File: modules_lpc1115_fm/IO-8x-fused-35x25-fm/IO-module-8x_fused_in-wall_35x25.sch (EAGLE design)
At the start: 83 parts, among them IC1 LPC1115, IC2 ATAES132A-SHEQ-T, Q2 ASFL, U1 EEPROM, X3 MICROMATCH-10

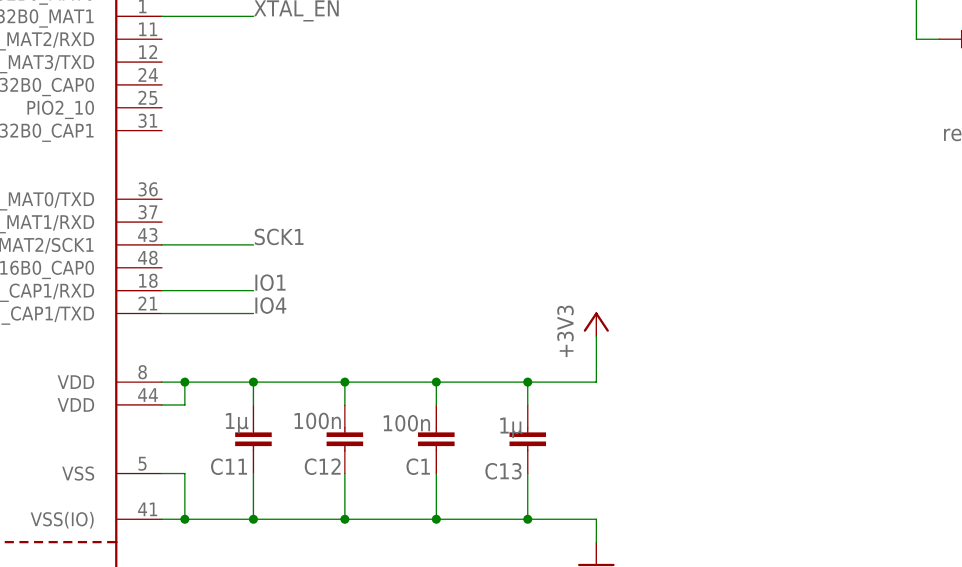
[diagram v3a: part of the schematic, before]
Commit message: [IOmodule8xUP] added debug RXD / TXD / GND solder pads
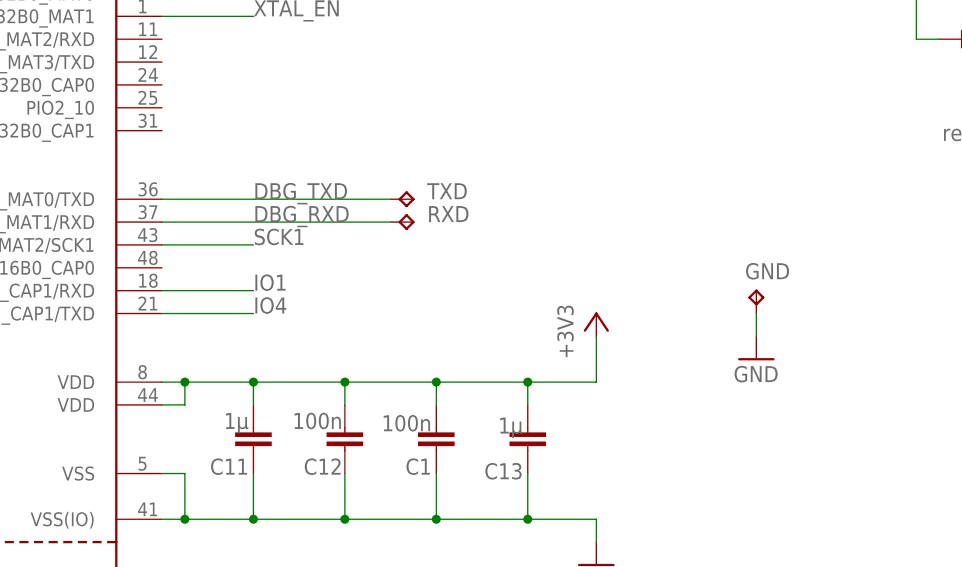
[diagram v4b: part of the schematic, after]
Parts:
- added GND: TPTP11SQ, testpad:TPTP11SQ
- added RXD: TPTP12R, testpad:TPTP12R
- added TXD: TPTP12SQ, testpad:TPTP12SQ
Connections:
- new net DBG_RXD: IC1.PIO3_1/DSR/CT16B0_MAT1/RXD, RXD.TP
- new net DBG_TXD: IC1.PIO3_0/DTR/CT16B0_MAT0/TXD, TXD.TP
- net GND: now also GND.TP
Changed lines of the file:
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@@
 <?xml version="1.0" encoding="utf-8"?>
 <!DOCTYPE eagle SYSTEM "eagle.dtd">
-<eagle version="9.6.1">
+<eagle version="9.6.2">
 <drawing>
 <settings>
@@
 <part name="P+12" library="supply1" deviceset="+3V3" device=""/>
 <part name="GND5" library="supply1" deviceset="GND" device=""/>
+<part name="TXD" library="testpad" library_urn="urn:adsk.eagle:library:385" deviceset="TP" device="TP12SQ" package3d_urn="urn:adsk.eagle:package:27964/1" value="TPTP12SQ"/>
+<part name="RXD" library="testpad" library_urn="urn:adsk.eagle:library:385" deviceset="TP" device="TP12R" package3d_urn="urn:adsk.eagle:package:27963/1" value="TPTP12R"/>
+<part name="GND" library="testpad" library_urn="urn:adsk.eagle:library:385" deviceset="TP" device="TP11SQ" package3d_urn="urn:adsk.eagle:package:27965/1" value="TPTP11SQ"/>
+<part name="GND7" library="supply1" deviceset="GND" device=""/>
 </parts>
 <sheets>
@@
 <instance part="GND5" gate="1" x="609.6" y="38.1" smashed="yes">
 <attribute name="VALUE" x="607.06" y="35.56" size="1.778" layer="96"/>
+</instance>
+<instance part="TXD" gate="G$1" x="434.34" y="137.16" smashed="yes" rot="R270">
+<attribute name="NAME" x="435.864" y="137.16" size="1.778" layer="95"/>
+<attribute name="TP_SIGNAL_NAME" x="433.07" y="135.89" size="1.778" layer="97" rot="R270"/>
+</instance>
+<instance part="RXD" gate="G$1" x="434.34" y="134.62" smashed="yes" rot="R270">
+<attribute name="NAME" x="435.864" y="134.62" size="1.778" layer="95"/>
+<attribute name="TP_SIGNAL_NAME" x="433.07" y="133.35" size="1.778" layer="97" rot="R270"/>
+</instance>
+<instance part="GND" gate="G$1" x="472.44" y="127" smashed="yes">
+<attribute name="NAME" x="471.17" y="128.27" size="1.778" layer="95"/>
+<attribute name="TP_SIGNAL_NAME" x="473.71" y="125.73" size="1.778" layer="97"/>
+</instance>
+<instance part="GND7" gate="1" x="472.44" y="119.38" smashed="yes">
+<attribute name="VALUE" x="469.9" y="116.84" size="1.778" layer="96"/>
 </instance>
 </instances>
@@
 <wire x1="523.24" y1="132.08" x2="523.24" y2="127" width="0.1524" layer="91"/>
 </segment>
+<segment>
+<pinref part="GND" gate="G$1" pin="TP"/>
+<pinref part="GND7" gate="1" pin="GND"/>
+<wire x1="472.44" y1="124.46" x2="472.44" y2="121.92" width="0.1524" layer="91"/>
+</segment>
 </net>
 <net name="EIB_OUT" class="0">
@@
 </segment>
 </net>
+<net name="DBG_TXD" class="0">
+<segment>
+<pinref part="IC1" gate="G$1" pin="PIO3_0/DTR/CT16B0_MAT0/TXD"/>
+<label x="416.56" y="137.16" size="1.778" layer="95"/>
+<wire x1="406.4" y1="137.16" x2="431.8" y2="137.16" width="0.1524" layer="91"/>
+<pinref part="TXD" gate="G$1" pin="TP"/>
+</segment>
+</net>
+<net name="DBG_RXD" class="0">
+<segment>
+<pinref part="IC1" gate="G$1" pin="PIO3_1/DSR/CT16B0_MAT1/RXD"/>
+<label x="416.56" y="134.62" size="1.778" layer="95"/>
+<wire x1="406.4" y1="134.62" x2="431.8" y2="134.62" width="0.1524" layer="91"/>
+<pinref part="RXD" gate="G$1" pin="TP"/>
+</segment>
+</net>

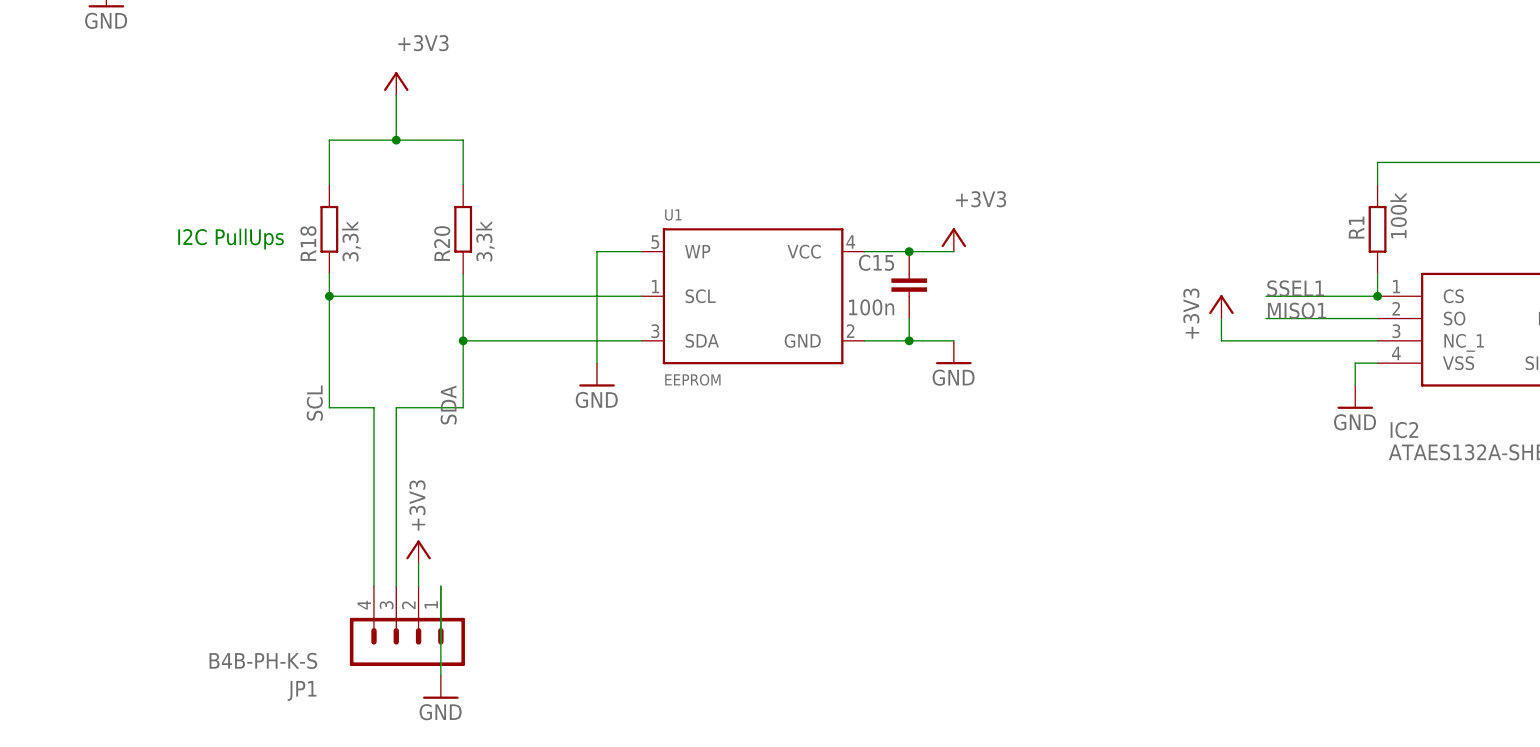
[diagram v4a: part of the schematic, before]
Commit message: [IOmodule8xUP] added missing blocking capacitor to IC2
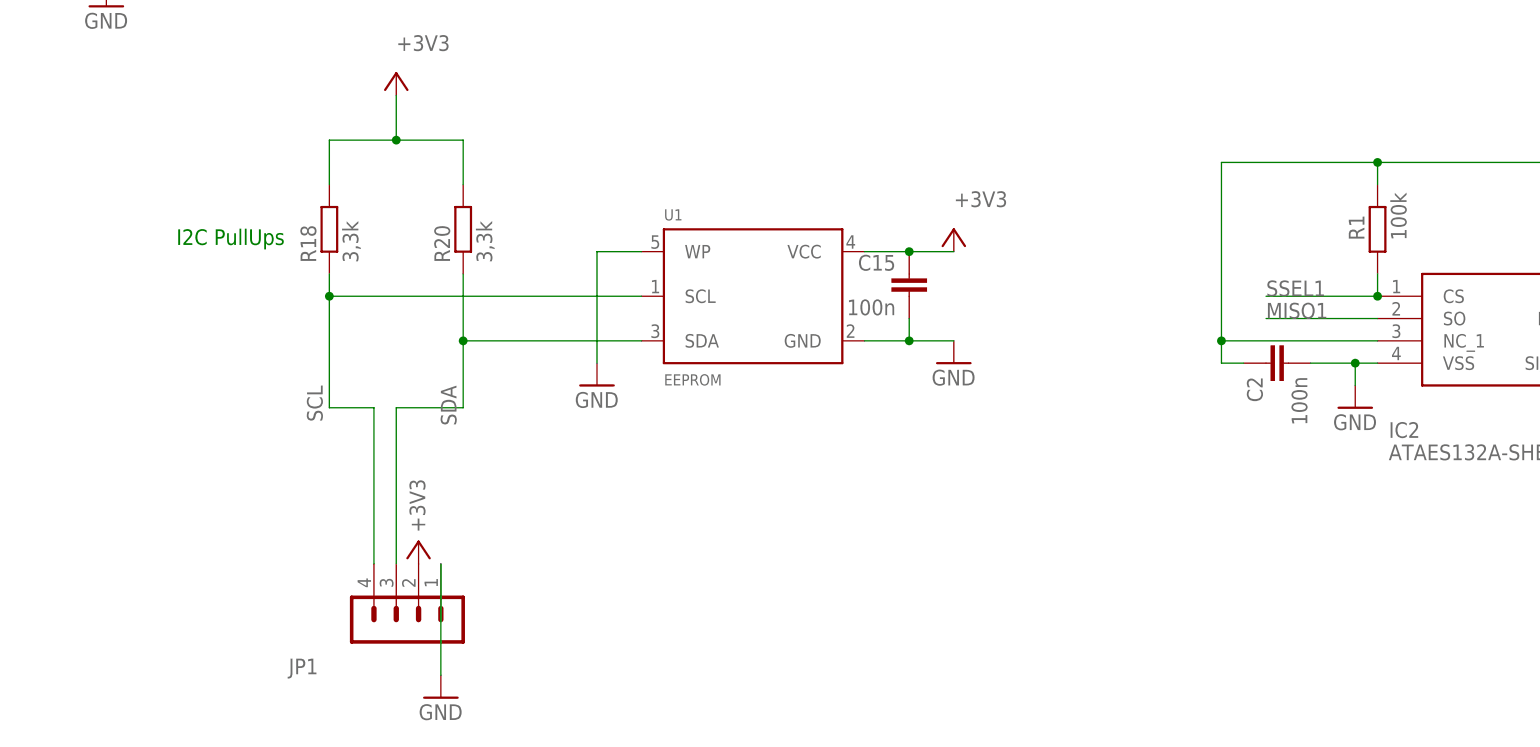
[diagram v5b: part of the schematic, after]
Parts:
- added C2: 100n, rcl:C-EUC0805
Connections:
- net +3V3: now also C2.1
- net GND: now also C2.2
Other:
- moved on the sheet: JP1
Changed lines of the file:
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@@
 </part>
 <part name="P+8" library="supply1" deviceset="+3V3" device=""/>
-<part name="JP1" library="con-JST PH" deviceset="B4B-PH" device="-K-S"/>
+<part name="JP1" library="con-JST PH" deviceset="B4B-PH" device="-K-S" value="B4B-PH-K-S"/>
 <part name="GND3" library="supply1" deviceset="GND" device=""/>
 <part name="P+3" library="supply1" deviceset="+3V3" device=""/>
@@
 <part name="PRGBTN" library="pinhead_dmx" deviceset="PINHD-1X1" device="" package3d_urn="urn:adsk.eagle:package:22485/2"/>
 <part name="GND4" library="supply1" deviceset="GND" device=""/>
-<part name="P+9" library="supply1" deviceset="+3V3" device=""/>
 <part name="P+12" library="supply1" deviceset="+3V3" device=""/>
 <part name="GND5" library="supply1" deviceset="GND" device=""/>
@@
 <part name="GND" library="testpad" library_urn="urn:adsk.eagle:library:385" deviceset="TP" device="TP11SQ" package3d_urn="urn:adsk.eagle:package:27965/1" value="TPTP11SQ"/>
 <part name="GND7" library="supply1" deviceset="GND" device=""/>
+<part name="C2" library="rcl" library_urn="urn:adsk.eagle:library:334" deviceset="C-EU" device="C0805" package3d_urn="urn:adsk.eagle:package:23617/2" value="100n">
+<spice>
+<pinmapping spiceprefix="C">
+<pinmap gate="G$1" pin="1" pinorder="1"/>
+<pinmap gate="G$1" pin="2" pinorder="2"/>
+</pinmapping>
+</spice>
+<attribute name="REICHELT" value="X7R-G0805 100N"/>
+</part>
 </parts>
 <sheets>
@@
 <attribute name="VALUE" x="553.72" y="134.62" size="1.778" layer="96" rot="R90"/>
 </instance>
-<instance part="JP1" gate="G$1" x="299.72" y="7.62" smashed="yes" rot="R90">
-<attribute name="NAME" x="290.83" y="4.445" size="1.778" layer="95" rot="R180"/>
-<attribute name="VALUE" x="290.83" y="7.62" size="1.778" layer="96" rot="R180"/>
+<instance part="JP1" gate="G$1" x="299.72" y="10.16" smashed="yes" rot="R90">
+<attribute name="NAME" x="290.83" y="6.985" size="1.778" layer="95" rot="R180"/>
 </instance>
 <instance part="GND3" gate="1" x="304.8" y="2.54" smashed="yes">
@@
 <attribute name="VALUE" x="520.7" y="121.92" size="1.778" layer="96"/>
 </instance>
-<instance part="P+9" gate="G$1" x="393.7" y="48.26" smashed="yes">
-<attribute name="VALUE" x="391.16" y="43.18" size="1.778" layer="96" rot="R90"/>
-</instance>
 <instance part="P+12" gate="G$1" x="485.14" y="55.88" smashed="yes">
 <attribute name="VALUE" x="482.6" y="50.8" size="1.778" layer="96" rot="R90"/>
@@
 <instance part="GND7" gate="1" x="472.44" y="119.38" smashed="yes">
 <attribute name="VALUE" x="469.9" y="116.84" size="1.778" layer="96"/>
+</instance>
+<instance part="C2" gate="G$1" x="398.78" y="40.64" smashed="yes" rot="MR270">
+<attribute name="REICHELT" x="398.78" y="40.64" size="1.778" layer="96" rot="MR270" display="off"/>
+<attribute name="NAME" x="398.399" y="39.116" size="1.778" layer="95" rot="MR270"/>
+<attribute name="VALUE" x="403.479" y="39.116" size="1.778" layer="96" rot="MR270"/>
 </instance>
 </instances>
@@
 <wire x1="411.48" y1="40.64" x2="408.94" y2="40.64" width="0.1524" layer="91"/>
 <wire x1="408.94" y1="40.64" x2="408.94" y2="38.1" width="0.1524" layer="91"/>
+<pinref part="C2" gate="G$1" pin="2"/>
+<wire x1="403.86" y1="40.64" x2="408.94" y2="40.64" width="0.1524" layer="91"/>
+<junction x="408.94" y="40.64"/>
 </segment>
 <segment>
@@
 <segment>
 <pinref part="GND3" gate="1" pin="GND"/>
-<wire x1="304.8" y1="15.24" x2="304.8" y2="5.08" width="0.1524" layer="91"/>
 <pinref part="JP1" gate="G$1" pin="1"/>
+<wire x1="304.8" y1="5.08" x2="304.8" y2="17.78" width="0.1524" layer="91"/>
 </segment>
 <segment>
@@
 </segment>
 <segment>
+<wire x1="38.1" y1="86.36" x2="27.94" y2="86.36" width="0.1524" layer="91"/>
+<label x="22.86" y="86.36" size="1.778" layer="95"/>
+<pinref part="X3" gate="-2" pin="S"/>
+</segment>
+<segment>
+<pinref part="P+3" gate="G$1" pin="+3V3"/>
+<pinref part="JP1" gate="G$1" pin="2"/>
+</segment>
+<segment>
+<pinref part="IC2" gate="G$1" pin="NC_1"/>
+<wire x1="411.48" y1="43.18" x2="393.7" y2="43.18" width="0.1524" layer="91"/>
+<pinref part="C2" gate="G$1" pin="1"/>
+<wire x1="396.24" y1="40.64" x2="393.7" y2="40.64" width="0.1524" layer="91"/>
+<wire x1="393.7" y1="40.64" x2="393.7" y2="43.18" width="0.1524" layer="91"/>
 <pinref part="IC2" gate="G$1" pin="VCC"/>
 <pinref part="P+7" gate="G$1" pin="+3V3"/>
@@
 <wire x1="444.5" y1="45.72" x2="444.5" y2="48.26" width="0.1524" layer="91"/>
 <junction x="444.5" y="48.26"/>
-</segment>
-<segment>
-<wire x1="38.1" y1="86.36" x2="27.94" y2="86.36" width="0.1524" layer="91"/>
-<label x="22.86" y="86.36" size="1.778" layer="95"/>
-<pinref part="X3" gate="-2" pin="S"/>
-</segment>
-<segment>
-<pinref part="P+3" gate="G$1" pin="+3V3"/>
-<pinref part="JP1" gate="G$1" pin="2"/>
-<wire x1="302.26" y1="17.78" x2="302.26" y2="15.24" width="0.1524" layer="91"/>
-</segment>
-<segment>
-<pinref part="IC2" gate="G$1" pin="NC_1"/>
-<wire x1="411.48" y1="43.18" x2="393.7" y2="43.18" width="0.1524" layer="91"/>
-<pinref part="P+9" gate="G$1" pin="+3V3"/>
-<wire x1="393.7" y1="45.72" x2="393.7" y2="43.18" width="0.1524" layer="91"/>
+<junction x="411.48" y="63.5"/>
+<wire x1="393.7" y1="63.5" x2="411.48" y2="63.5" width="0.1524" layer="91"/>
+<wire x1="393.7" y1="43.18" x2="393.7" y2="63.5" width="0.1524" layer="91"/>
+<junction x="393.7" y="43.18"/>
 </segment>
 </net>
@@
 <wire x1="292.1" y1="35.56" x2="297.18" y2="35.56" width="0.1524" layer="91"/>
 <pinref part="JP1" gate="G$1" pin="4"/>
-<wire x1="297.18" y1="35.56" x2="297.18" y2="15.24" width="0.1524" layer="91"/>
+<wire x1="297.18" y1="35.56" x2="297.18" y2="17.78" width="0.1524" layer="91"/>
 </segment>
 </net>
@@
 <wire x1="307.34" y1="35.56" x2="299.72" y2="35.56" width="0.1524" layer="91"/>
 <pinref part="JP1" gate="G$1" pin="3"/>
-<wire x1="299.72" y1="35.56" x2="299.72" y2="15.24" width="0.1524" layer="91"/>
-</segment>
-</net>
+<wire x1="299.72" y1="35.56" x2="299.72" y2="17.78" width="0.1524" layer="91"/>
+</segment>
+</net>
